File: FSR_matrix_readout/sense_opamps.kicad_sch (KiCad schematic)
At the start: 44 parts, among them U18 TLV9064, U19 TLV9064, U20 TLV9064, U3 TLV9064

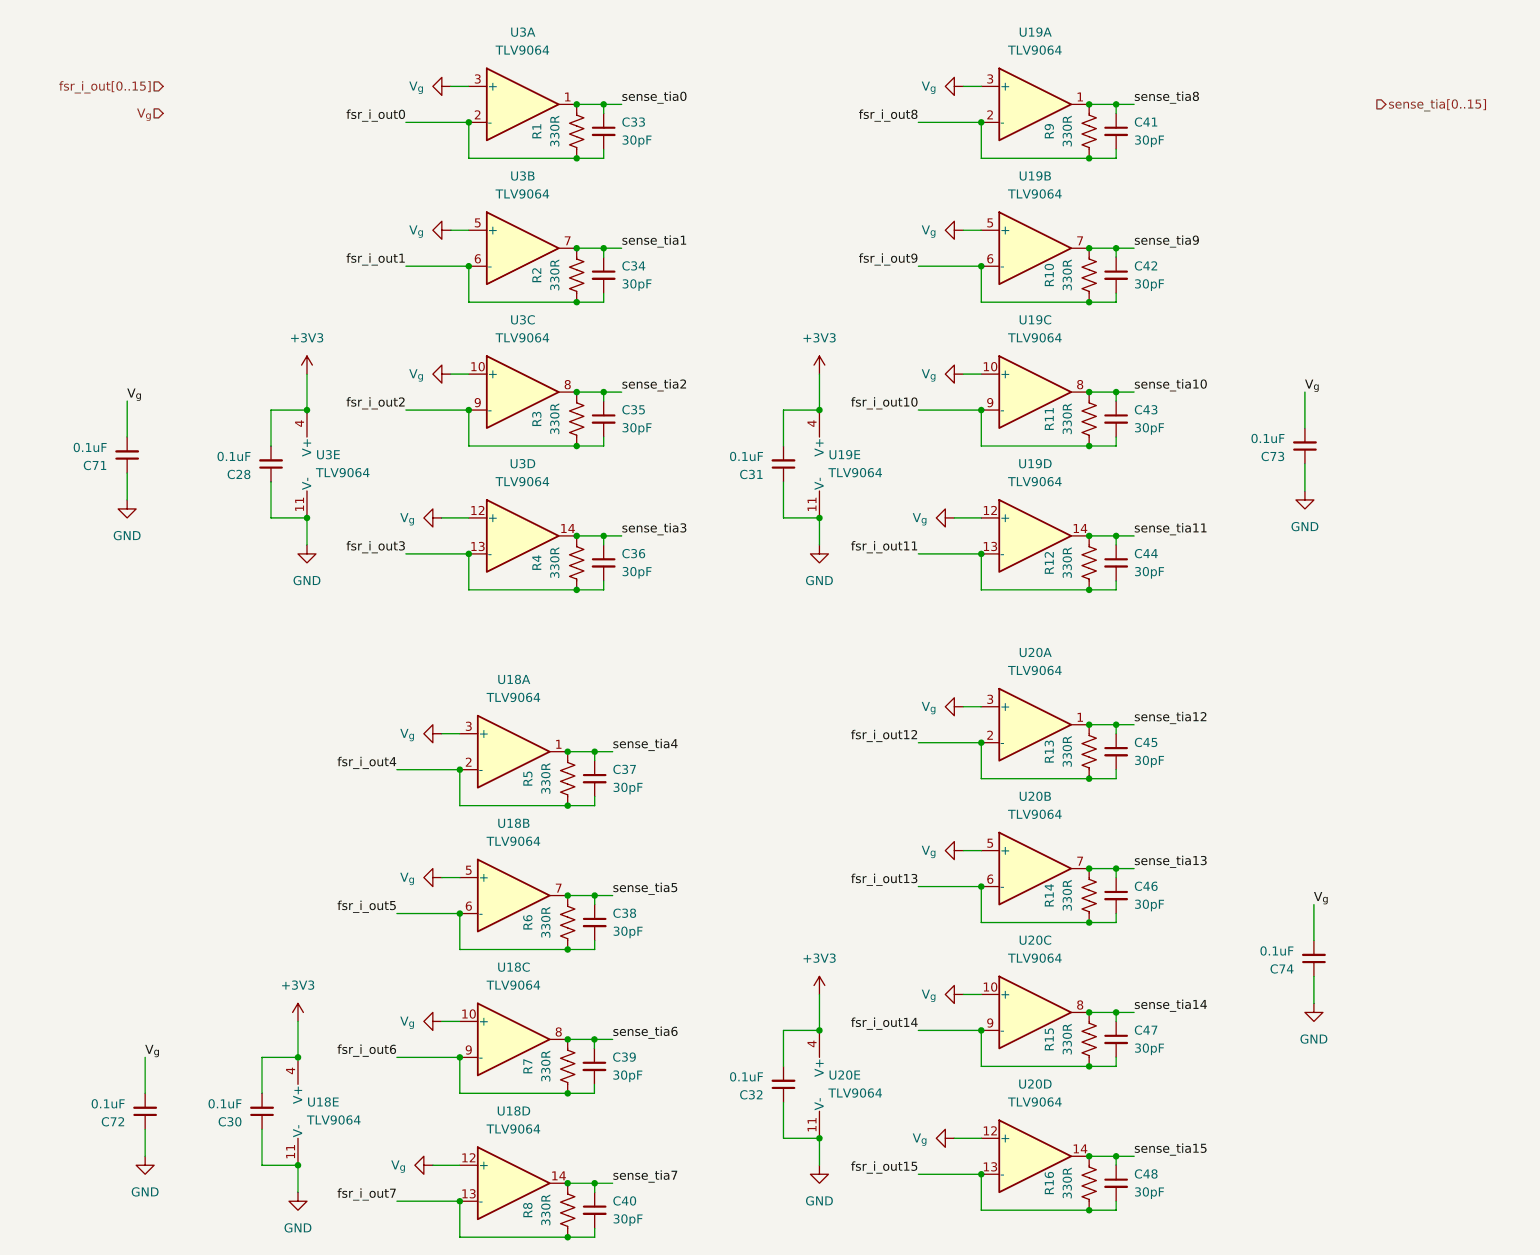
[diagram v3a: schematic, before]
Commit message: remove all ERC errors
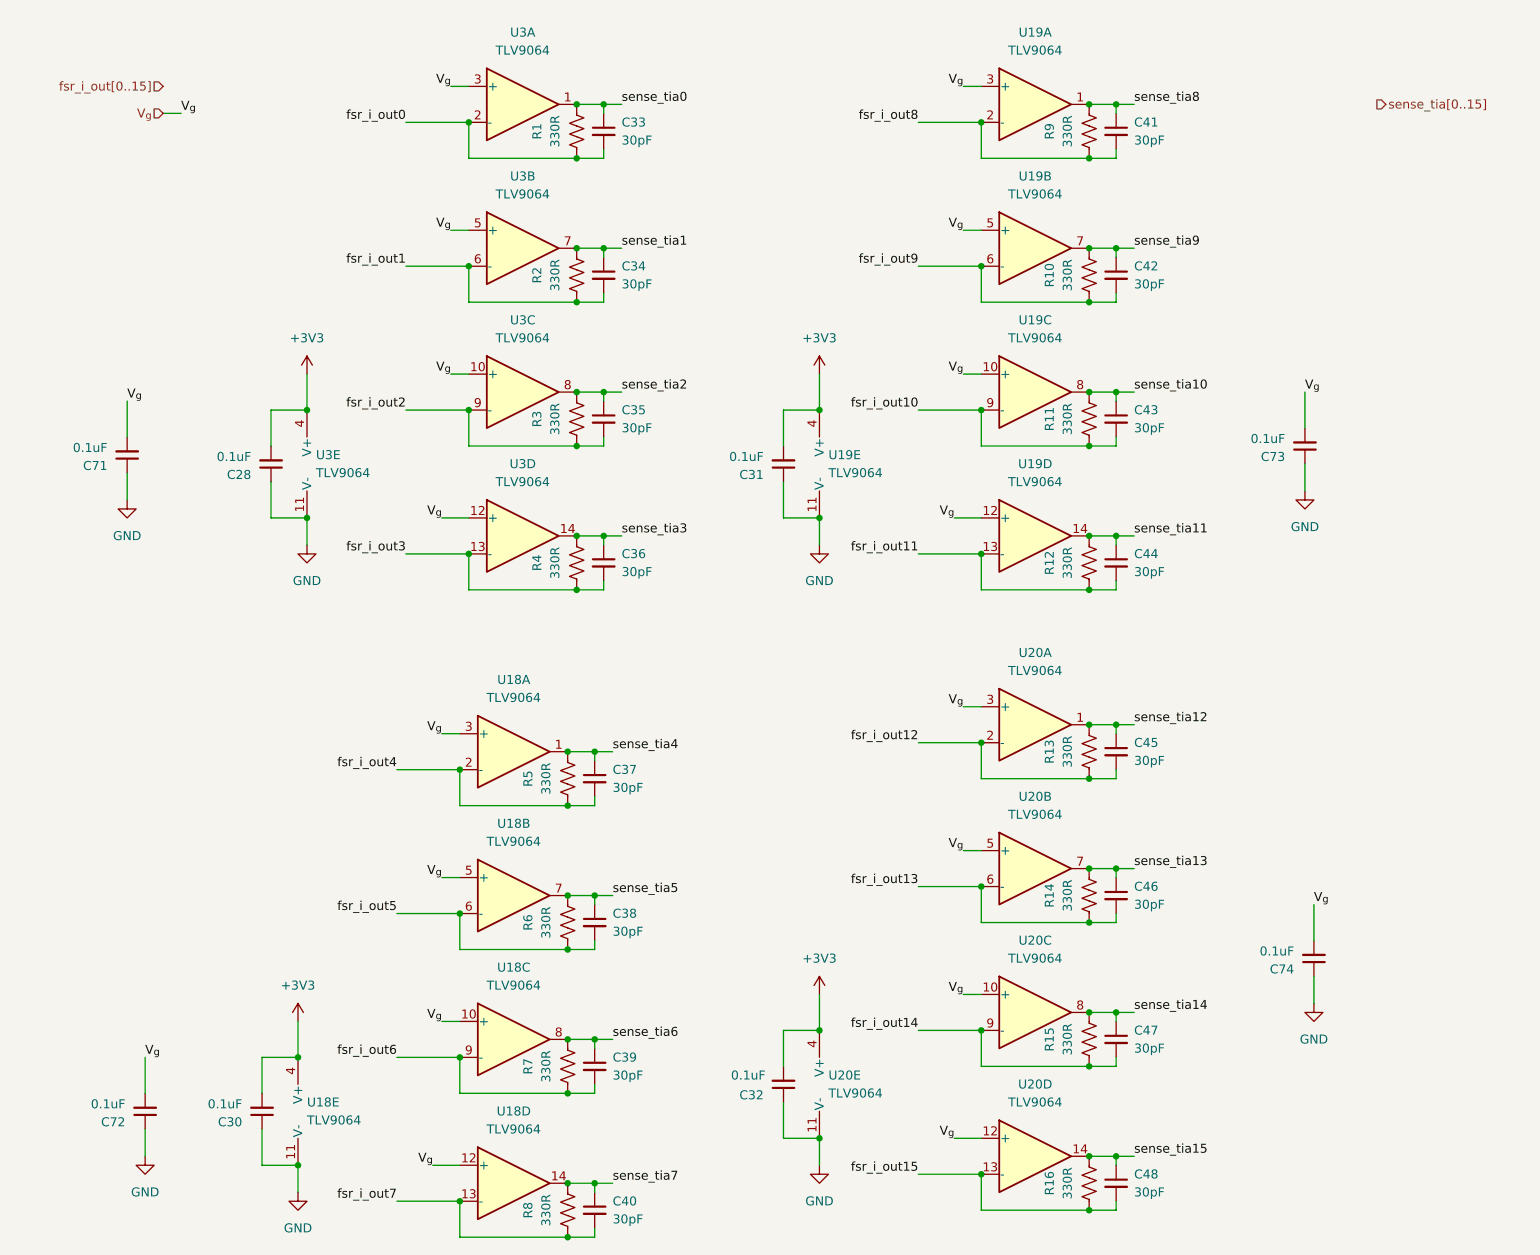
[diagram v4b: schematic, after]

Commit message: added some test points
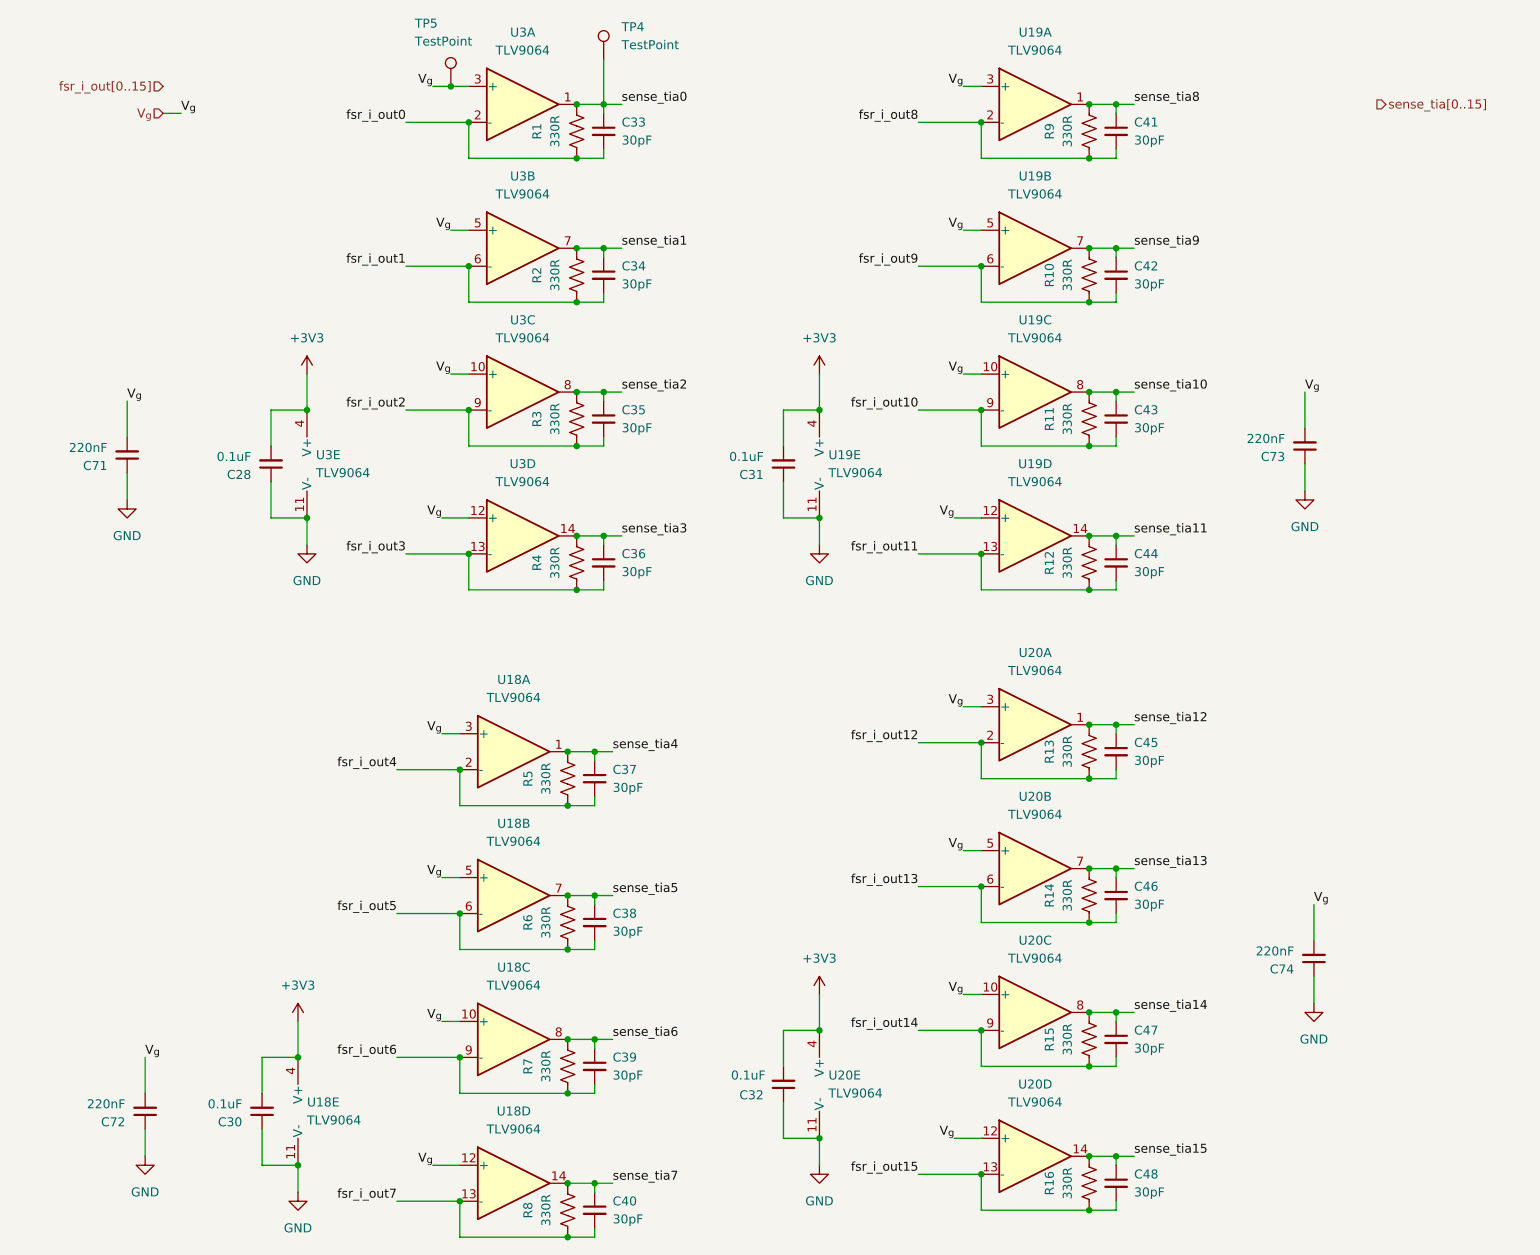
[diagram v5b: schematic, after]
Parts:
- added TP4, TP5: TestPoint, symbol Connector:TestPoint
- C71, C72, C73, C74: value 0.1uF -> 220nF
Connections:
- net V_{g}: now also TP5.1
- net sense_tia0: now also TP4.1
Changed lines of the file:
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@@
 	)
 	(junction
+		(at 76.2 29.21)
+		(diameter 0)
+		(color 0 0 0 0)
+	)
+	(junction
 		(at 96.52 184.15)
 		(diameter 0)
@@
 	(wire
 		(pts
-			(xy 76.2 29.21) (xy 78.74 29.21)
+			(xy 73.66 29.21) (xy 76.2 29.21)
 		)
 		(stroke
@@
 	(wire
 		(pts
+			(xy 97.79 25.4) (xy 97.79 31.75)
+		)
+		(stroke
+			(width 0)
+			(type default)
+		)
+	)
+	(wire
+		(pts
 			(xy 128.27 90.17) (xy 128.27 93.98)
 		)
@@
 	(wire
 		(pts
+			(xy 76.2 29.21) (xy 78.74 29.21)
+		)
+		(stroke
+			(width 0)
+			(type default)
+		)
+	)
+	(wire
+		(pts
 			(xy 166.37 52.07) (xy 170.18 52.07)
 		)
@@
 	)
 	(label "V_{g}"
-		(at 76.2 29.21 180)
+		(at 73.66 29.21 180)
 		(effects
 			(font
@@
 			)
 		)
-		(property "Value" "0.1uF"
+		(property "Value" "220nF"
 			(at 27.686 80.264 0)
 			(show_name no)
@@
 	)
 	(symbol
+		(lib_id "Connector:TestPoint")
+		(at 76.2 29.21 0)
+		(unit 1)
+		(body_style 1)
+		(exclude_from_sim no)
+		(in_bom yes)
+		(on_board yes)
+		(in_pos_files yes)
+		(dnp no)
+		(property "Reference" "TP5"
+			(at 71.12 20.32 0)
+			(show_name no)
+			(do_not_autoplace no)
+			(effects
+				(font
+					(size 1.27 1.27)
+				)
+				(justify left)
+			)
+		)
+		(property "Value" "TestPoint"
+			(at 71.12 22.86 0)
+			(show_name no)
+			(do_not_autoplace no)
+			(effects
+				(font
+					(size 1.27 1.27)
+				)
+				(justify left)
+			)
+		)
+		(property "Footprint" ""
+			(at 81.28 29.21 0)
+			(hide yes)
+			(show_name no)
+			(do_not_autoplace no)
+			(effects
+				(font
+					(size 1.27 1.27)
+				)
+			)
+		)
+		(property "Datasheet" ""
+			(at 81.28 29.21 0)
+			(hide yes)
+			(show_name no)
+			(do_not_autoplace no)
+			(effects
+				(font
+					(size 1.27 1.27)
+				)
+			)
+		)
+		(property "Description" "test point"
+			(at 76.2 29.21 0)
+			(hide yes)
+			(show_name no)
+			(do_not_autoplace no)
+			(effects
+				(font
+					(size 1.27 1.27)
+				)
+			)
+		)
+		(pin "1"
+		)
+		(instances
+			(project "FSR_matrix_readout"
+				(path "/6dca5e5c-f676-465d-98c9-14af6047a226/bd0ecfe5-c384-4745-b841-51e834c1c1f6"
+					(reference "TP5")
+					(unit 1)
+				)
+			)
+		)
+	)
+	(symbol
 		(lib_id "Device:C_Small")
 		(at 97.79 55.88 0)
@@
 			)
 		)
-		(property "Value" "0.1uF"
+		(property "Value" "220nF"
 			(at 30.226 172.974 0)
 			(show_name no)
@@
 			)
 		)
-		(property "Value" "0.1uF"
+		(property "Value" "220nF"
 			(at 195.326 151.384 0)
 			(show_name no)
@@
 			)
 		)
-		(property "Value" "0.1uF"
+		(property "Value" "220nF"
 			(at 194.056 78.994 0)
 			(show_name no)
@@
 					(unit 1)
 				)
+			)
+		)
+	)
+	(symbol
+		(lib_id "Connector:TestPoint")
+		(at 97.79 25.4 0)
+		(unit 1)
+		(body_style 1)
+		(exclude_from_sim no)
+		(in_bom yes)
+		(on_board yes)
+		(in_pos_files yes)
+		(dnp no)
+		(fields_autoplaced yes)
+		(property "Reference" "TP4"
+			(at 100.33 20.8279 0)
+			(show_name no)
+			(do_not_autoplace no)
+			(effects
+				(font
+					(size 1.27 1.27)
+				)
+				(justify left)
+			)
+		)
+		(property "Value" "TestPoint"
+			(at 100.33 23.3679 0)
+			(show_name no)
+			(do_not_autoplace no)
+			(effects
+				(font
+					(size 1.27 1.27)
+				)
+				(justify left)
+			)
+		)
+		(property "Footprint" ""
+			(at 102.87 25.4 0)
+			(hide yes)
+			(show_name no)
+			(do_not_autoplace no)
+			(effects
+				(font
+					(size 1.27 1.27)
+				)
+			)
+		)
+		(property "Datasheet" ""
+			(at 102.87 25.4 0)
+			(hide yes)
+			(show_name no)
+			(do_not_autoplace no)
+			(effects
+				(font
+					(size 1.27 1.27)
+				)
+			)
+		)
+		(property "Description" "test point"
+			(at 97.79 25.4 0)
+			(hide yes)
+			(show_name no)
+			(do_not_autoplace no)
+			(effects
+				(font
+					(size 1.27 1.27)
+				)
+			)
+		)
+		(pin "1"
+		)
+		(instances
+			(project "FSR_matrix_readout"
+				(path "/6dca5e5c-f676-465d-98c9-14af6047a226/bd0ecfe5-c384-4745-b841-51e834c1c1f6"
+					(reference "TP4")
+					(unit 1)
+				)
